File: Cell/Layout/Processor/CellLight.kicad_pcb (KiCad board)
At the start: 2 copper layers, 100 x 16 mm, 30 parts, among them J1 Conn_01x05, J2 Conn_01x02, J3 Conn_01x02, J4 Conn_01x02, J5 Conn_01x03, J6 Conn_01x03, SW1 SW_Push, U1 STM32G030F6P6, U10 74LVC1G125, U11 LM1085-5.0, U2 74LVC1G125, U3 MB85RC256, U4 74LVC1G125, U5 AP2112K-3.3, U6 SN74LVC1T45DBVR, U7 74LVC1G125, U8 74LVC1G125, U9 74LVC1G125

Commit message: Do the processor board layout
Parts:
- removed D1: DF02M, Diode_THT:Diode_Bridge_DIP-4_W7.62mm_P5.08mm
- removed the U5 at (149.4, 130.2)
- added CR1: DF01S, df01s:DF01S, F.Cu at (130.0, 133.6)
- added U11: AP2112K-3.3, Package_TO_SOT_SMD:SOT-23-5, F.Cu at (162.0, 139.7)
- moved J4 21.4 mm to (120.5, 130.0)
- moved J2 17.5 mm to (139.4, 130.0)
- moved C5 17.3 mm to (164.9, 139.7)
- moved C6 17.1 mm to (166.6, 139.7)
- moved R1 14.9 mm to (175.8, 130.5), turned to 270 degrees
- moved R2 14.9 mm to (175.2, 136.1), turned to 90 degrees
- moved J1 14.8 mm to (162.8, 128.7), turned to 270 degrees
- moved U10 13.8 mm to (151.5, 135.8)
- moved U2 11.9 mm to (180.6, 136.1)
- moved C4 11.1 mm to (148.6, 129.0), turned to 180 degrees
- moved U9 9.89 mm to (171.3, 136.8)
- moved SW1 6.08 mm to (165.9, 134.2), turned to 0 degrees
- moved R3 5.96 mm to (160.7, 133.2), turned to 270 degrees
- moved C2 4.71 mm to (136.1, 139.2)
- moved C1 3.74 mm to (138.9, 139.2)
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- renumbered C7 to C1, C8 to C2, C9 to C3, C10 to C4, C11 to C5, C1 to C6, R2 to R1, R3 to R2, R1 to R3, U6 to U1, U11 to U10, U1 to U2, U2 to U3, U7 to U5, U8 to U6, U9 to U7, U10 to U8, U3 to U9
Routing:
- net CH1_RX_EN: track 47.3 -> 4.65 mm
- net 3.3V: track 116.0 -> 148.4 mm, vias 1 -> 2
- net SWCLK: track 43.0 -> 13.6 mm, vias 1 -> 0
- net CH1_DATA: track 52.6 -> 26.2 mm
- net COM_DATA: track 49.9 -> 67.9 mm, vias 2 -> 1
- net CH2_DATA: track 33.2 -> 46.1 mm, vias 1 -> 2
- net NRST: track 21.9 -> 33.4 mm
- net CH2_TX_EN: track 30.4 -> 20.5 mm
- net GND: track 216.5 -> 225.5 mm, vias 0 -> 2
- net CH1_TX_EN: track 27.6 -> 19.9 mm
- net CH3_DATA: track 36.4 -> 43.9 mm
- net CH3_TX_EN: track 25.3 -> 18.1 mm
- net PRI_LO: track 26.6 -> 31.5 mm, vias 0 -> 1
- net Net-(U1-Pad4): track 25.6 -> 30.3 mm
- net SWDIO: track 21.8 -> 17.1 mm, vias 1 -> 0
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- added copper zone on F.Cu, net 5V
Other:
- board size 100 x 16 mm -> 100 x 15 mm

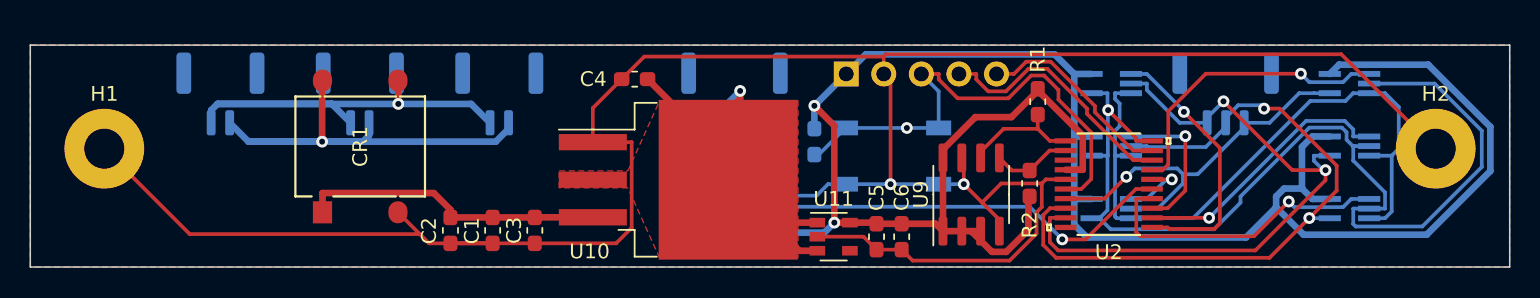
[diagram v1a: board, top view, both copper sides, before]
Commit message: Finish layouts
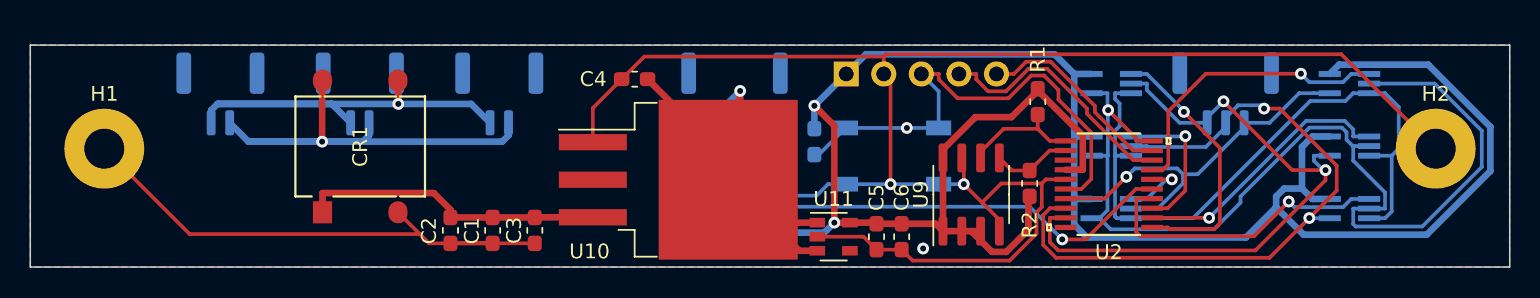
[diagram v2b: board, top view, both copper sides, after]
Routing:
- net GND: track 225.5 -> 210.1 mm, vias 2 -> 3
- removed copper zone on F.Cu, net 5V
